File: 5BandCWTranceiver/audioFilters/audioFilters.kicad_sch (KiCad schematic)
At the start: 45 parts

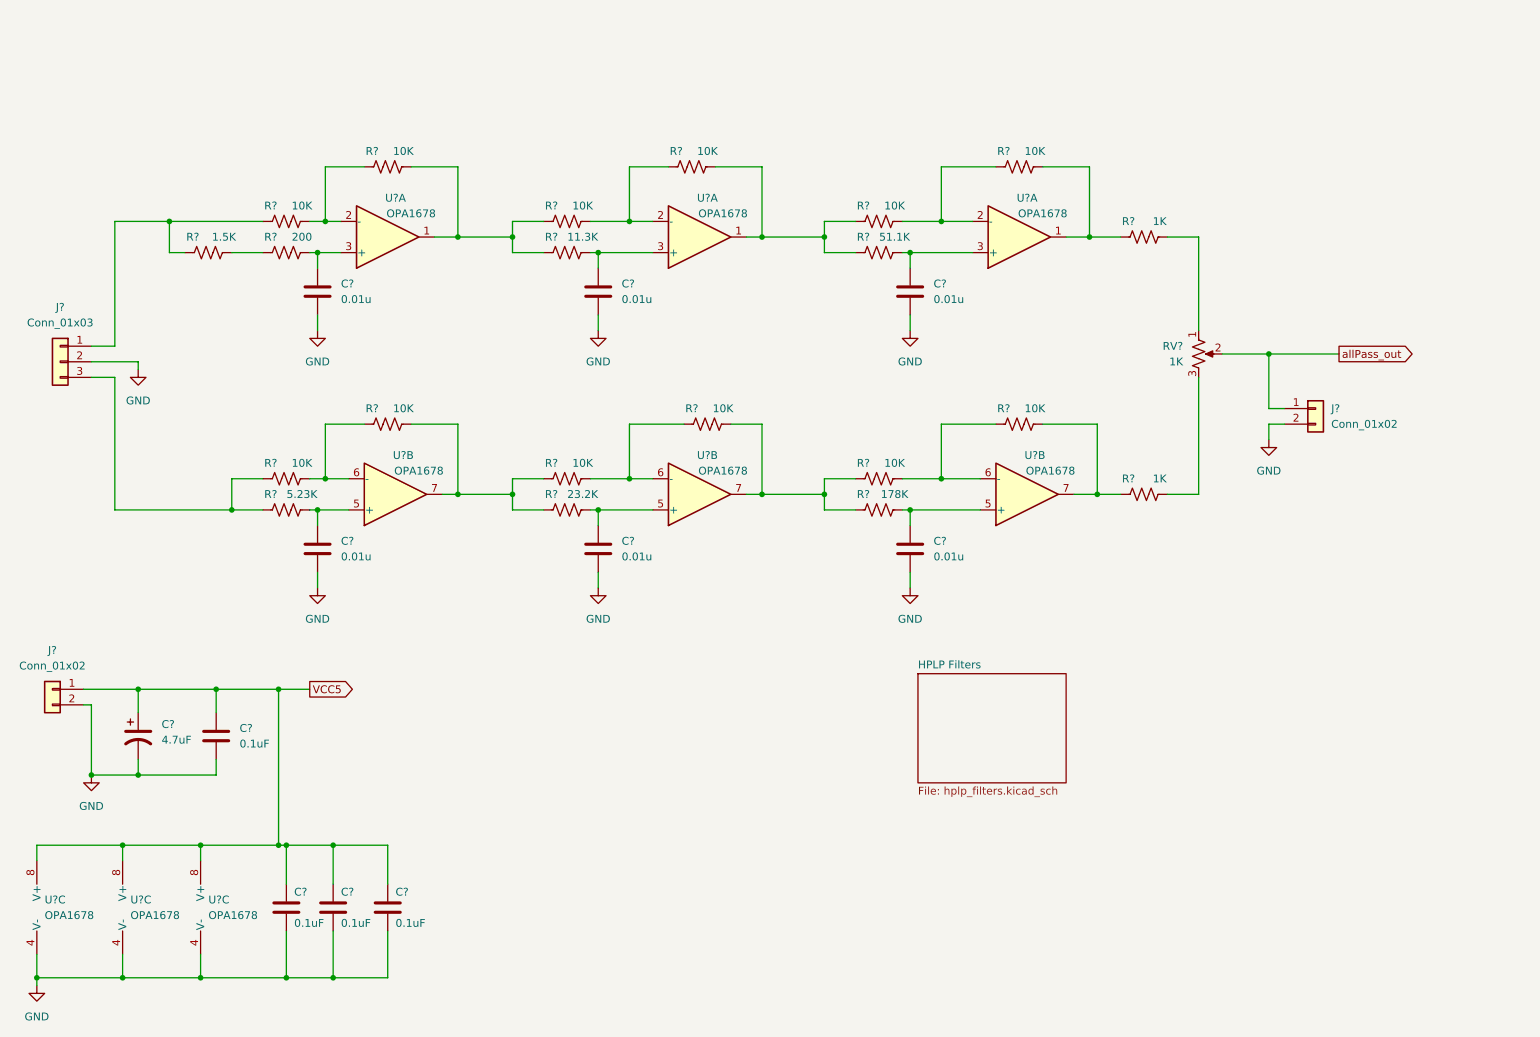
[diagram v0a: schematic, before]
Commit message: Start allpass+filters
Initial commit of board combining allpass and hp, lp filters
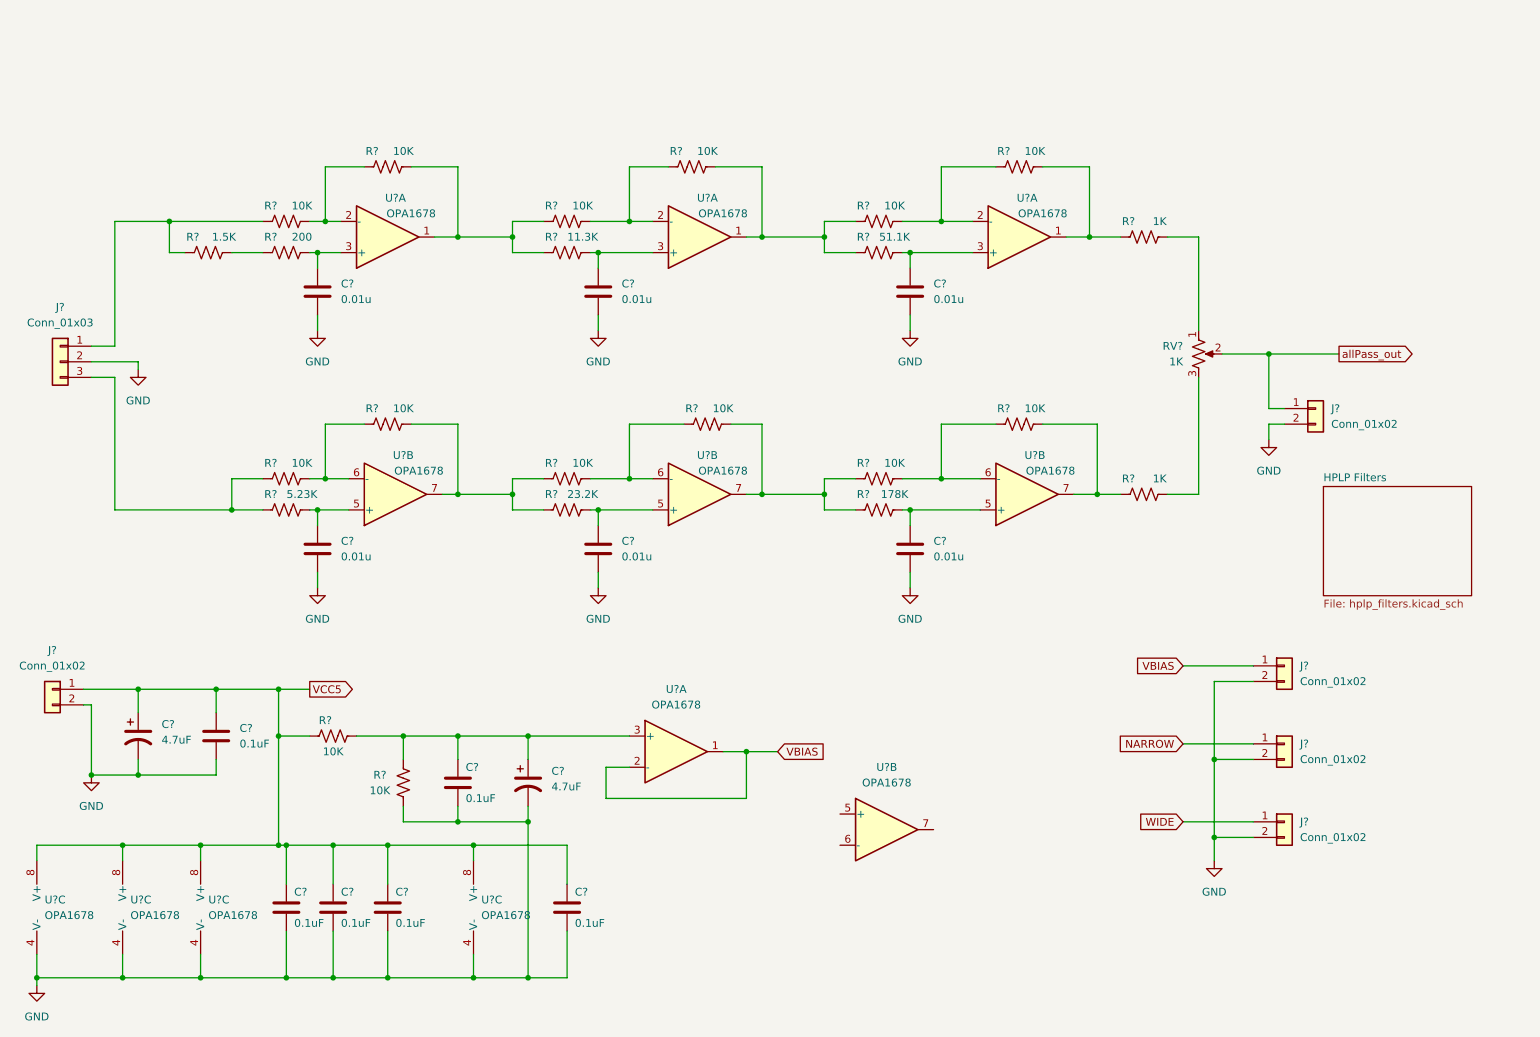
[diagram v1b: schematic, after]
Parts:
- added C? (x2): 0.1uF, Capacitor_SMD:C_0603_1608Metric_Pad1.08x0.95mm_HandSolder, symbol Device:C
- added C?: 4.7uF, Capacitor_THT:CP_Radial_D5.0mm_P2.50mm, symbol Device:C_Polarized_US
- added J? (x3): Conn_01x02, Connector_PinHeader_2.54mm:PinHeader_1x02_P2.54mm_Vertical, symbol Connector_Generic:Conn_01x02
- added R? (x2): 10K, Resistor_SMD:R_0603_1608Metric_Pad0.98x0.95mm_HandSolder, symbol Device:R_US
- added U? (x2): OPA1678, Package_SO:SOIC-8_3.9x4.9mm_P1.27mm, symbol Amplifier_Operational:OPA1678
- added U?: OPA1678, symbol Amplifier_Operational:OPA1678
- U? (x3): footprint (none) -> Package_SO:SOIC-8_3.9x4.9mm_P1.27mm
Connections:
- net GND: now also C?.2, C?.2, C?.2, J?.2 (Pin_2), J?.2 (Pin_2), J?.2 (Pin_2), R?.1, U?.4 (V-)
- net VCC5: now also C?.1, R?.1, U?.8 (V+)
- new net: C?.1, C?.1, R?.2, R?.2, U?.3 (+)
- new net NARROW: J?.1 (Pin_1)
- new net VBIAS: J?.1 (Pin_1), U?.1, U?.2 (-)
- new net WIDE: J?.1 (Pin_1)

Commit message: Initial Placement
Initial placement of audio filter board
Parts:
- gave numbers to parts that had none: 48
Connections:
- net VBIAS: now also U4.1, U4.2 (-); no longer U2.1, U2.2 (-)
- net allPass_out: now also U4.6 (-), U4.7; no longer RV1.2
- net at U4.5 (+): now also RV1.2
- net at R20.2, R22.1: now also U3.1; no longer U4.1
- net at R10.2, R14.1: now also U2.2 (-); no longer U3.2 (-)
- net at R14.2, R16.1, R17.1: now also U2.1; no longer U3.1
- net at C11.1, R11.2: now also U2.3 (+); no longer U3.3 (+)
- net at C13.1, R17.2: now also U3.3 (+); no longer U4.3 (+)
- net at C8.1, C9.1, R6.2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: now also U4.3 (+); no longer U2.3 (+)
- net at R16.2, R20.1: now also U3.2 (-); no longer U4.2 (-)
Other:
- note added: "All Pass Filter and Wide/Narrow Audio Filters"
- moved on the sheet: J6, U2A, U3A, U4A, U4B

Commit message: audioFilters board tapeout
ready for tapeout
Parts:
- added J10, J7, J8, J9: Conn_01x02, Connector_PinHeader_2.54mm:PinHeader_1x02_P2.54mm_Vertical, symbol Connector_Generic:Conn_01x02
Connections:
- net GND: now also J10.1 (Pin_1), J10.2 (Pin_2), J7.1 (Pin_1), J7.2 (Pin_2), J8.1 (Pin_1), J8.2 (Pin_2), J9.1 (Pin_1), J9.2 (Pin_2)
